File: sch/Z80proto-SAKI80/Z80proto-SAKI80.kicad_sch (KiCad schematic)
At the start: 21 parts, among them SW2 ABORT, U2 HC74, U20 AC00, U3 HC14, U7 2764, U8 628128, U9 HC138, X1 ACO-4.000MHz

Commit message: add SAKI80 support
add SAKI80(AKA Super AKI-80) support,
Modify Comand & intel HEX upload command to MiniLoader.
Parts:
- removed U3: HC14, symbol 74xx:74HC14
- removed X1: ACO-4.000MHz, Oscillator:Oscillator_DIP-14, symbol Oscillator:ACO-xxxMHz
- added U3: HC14, symbol 74xx:74LS14
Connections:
- net BUSAK*: now also U20.10
- net BUSNMI*: now also U3.3
- net BUSRES*: now also U3.11
- net BUSφ: now also U3.2
- net CPUφ: now also U3.13
- net GND: now also U3.10, U3.7 (GND), U3.9; no longer U20.1, U20.10, U20.2, U20.9
- net HALT: now also U20.3; no longer U20.11
- net HALT*: now also U20.1, U20.2; no longer U20.12, U20.13
- net NMI*: now also U3.6
- net RESET: now also U3.10, U3.9
- net VCC: now also U3.14 (VCC)
- net WR*: now also U20.12, U20.13
- net SYSRESET* renamed P3
- net P3: now also U3.8
- new net: U20.11, U20.9
- new net: U3.1, U3.12
- new net: U3.4, U3.5
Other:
- note added: "(or 2816)"
- note added: "26"
- note added: "A11(WR*)"
- note added: "Experimental: ROMKICK"
- note added: "NC(VCC)"
- note removed: "26(24)"
- note removed: "Evaluation: ROMKICK"
- moved on the sheet: C2, D2, R4, R5, SW2, U20A, U20C, U20D

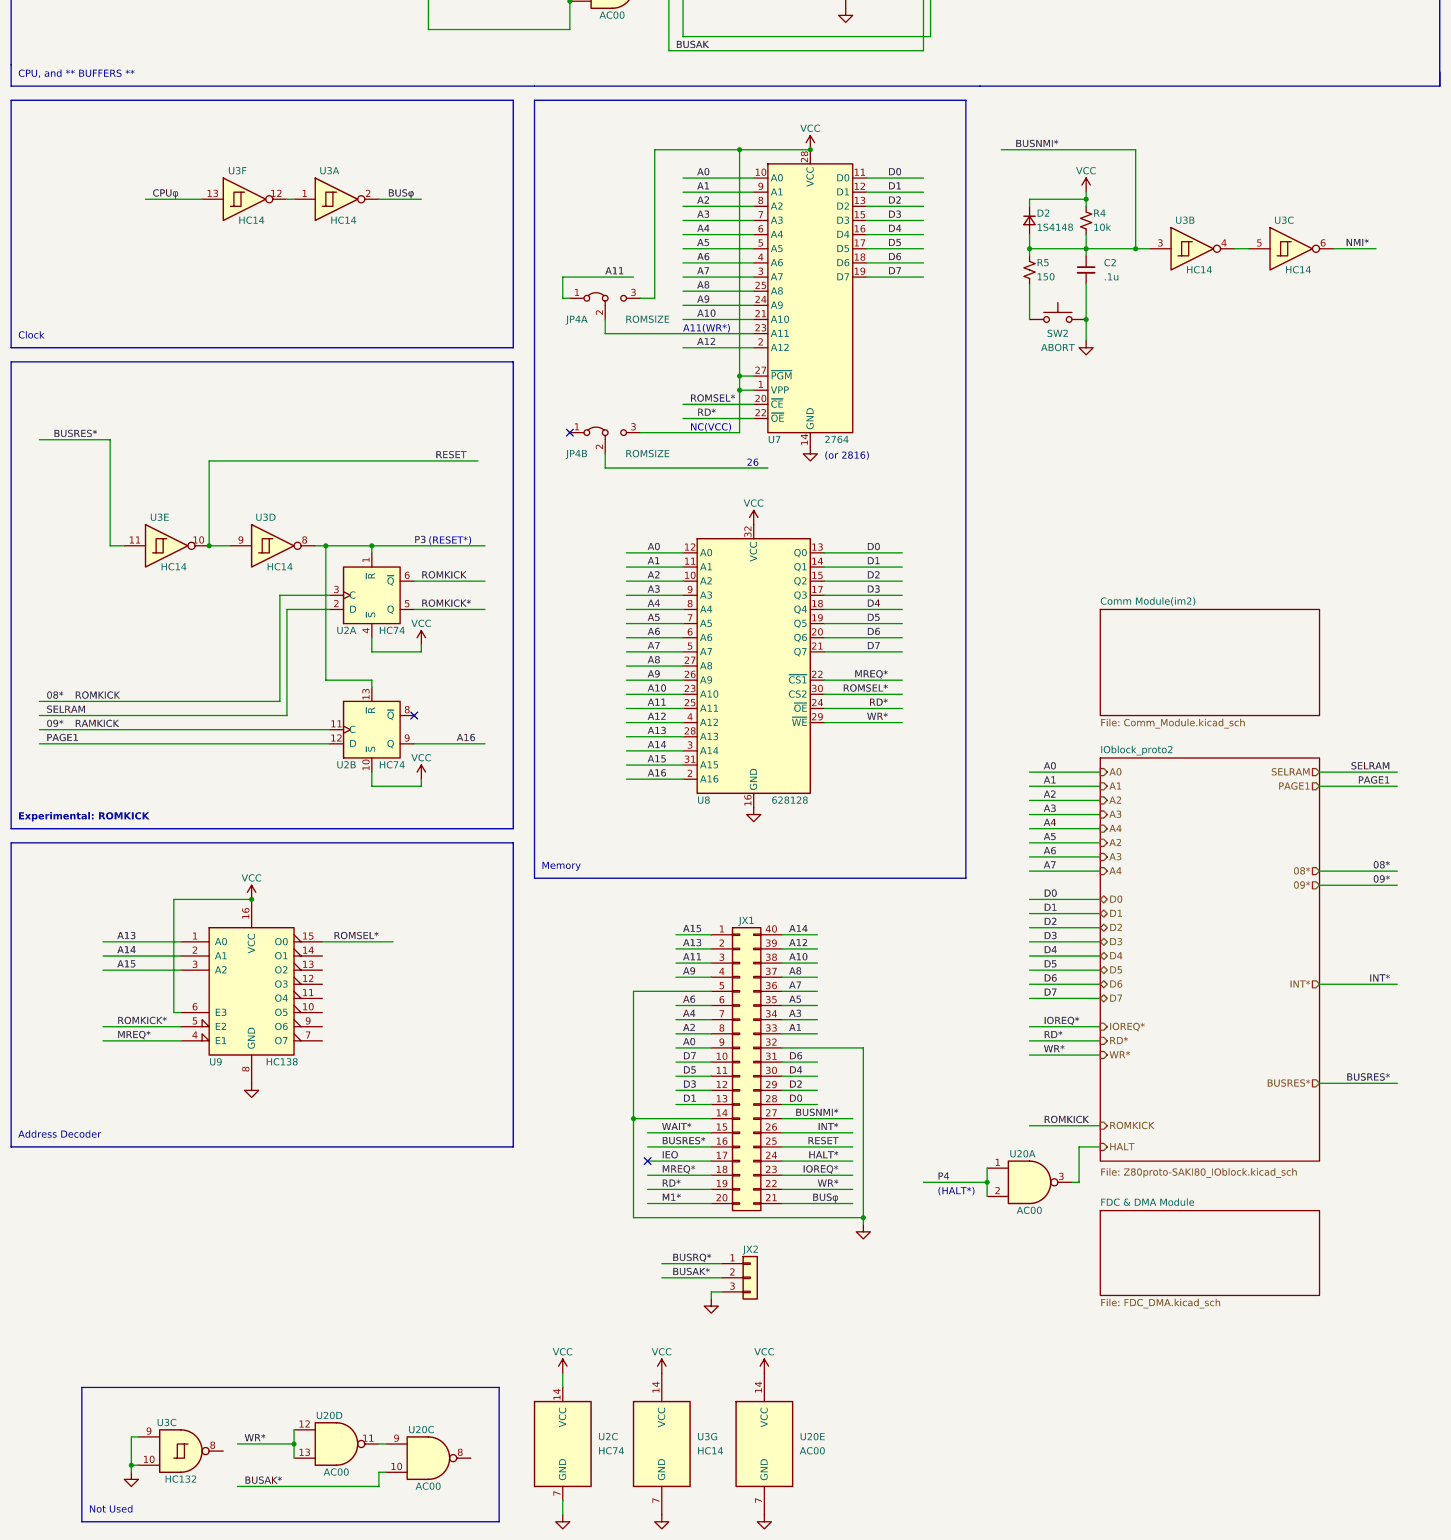
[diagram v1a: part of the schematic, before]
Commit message: add misc.
add SIO Hard flow control(but not work ...),
add WAIT implement,
add kermit implement(test).
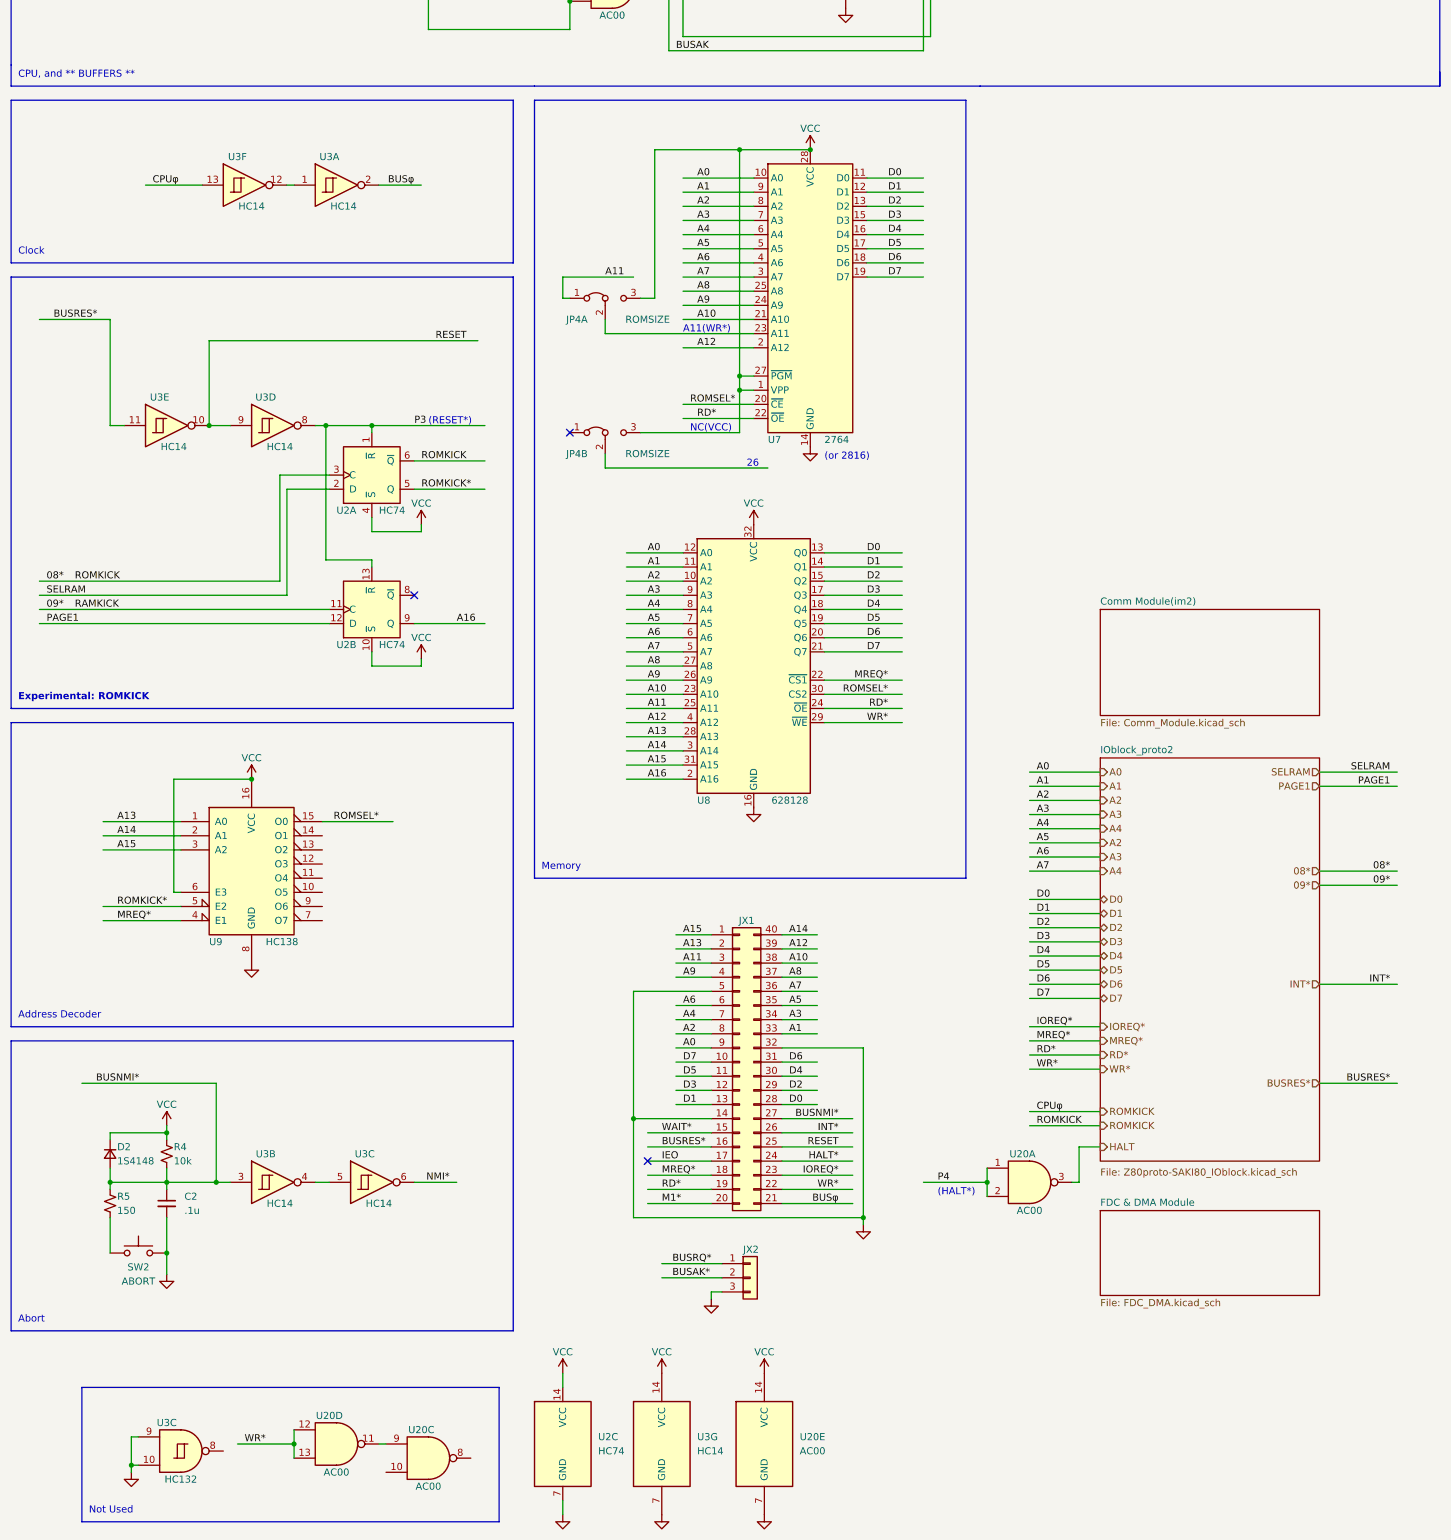
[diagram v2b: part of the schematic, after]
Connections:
- net CPUφ is gone; now on net 08*: U3.13, UB1.2 (~{CLKOUT})
- net BUSAK*: no longer U20.10
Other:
- note added: "Abort"
- moved on the sheet: C2, D2, R4, R5, SW2, U2A, U2B, U3A, U3B, U3C, U3D, U3E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

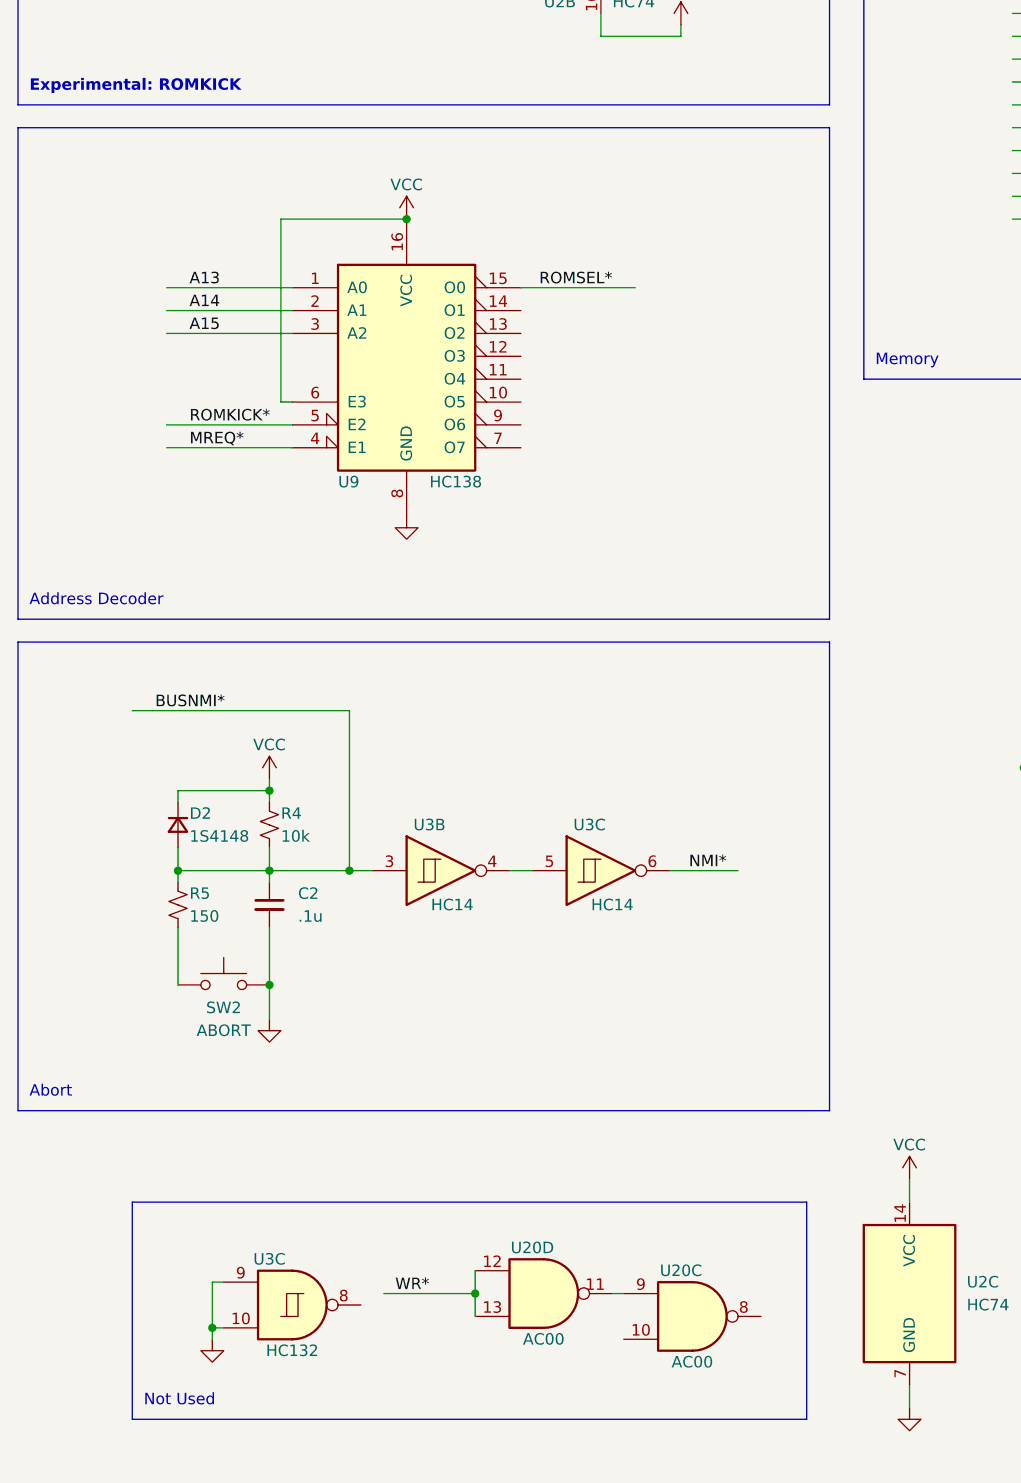
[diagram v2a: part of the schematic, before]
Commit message: patch xymodem.c and command_x.asm
add putchar_SIO0()/getchar_SIO0(), and SlowTick, SysTick
fix file title, comments
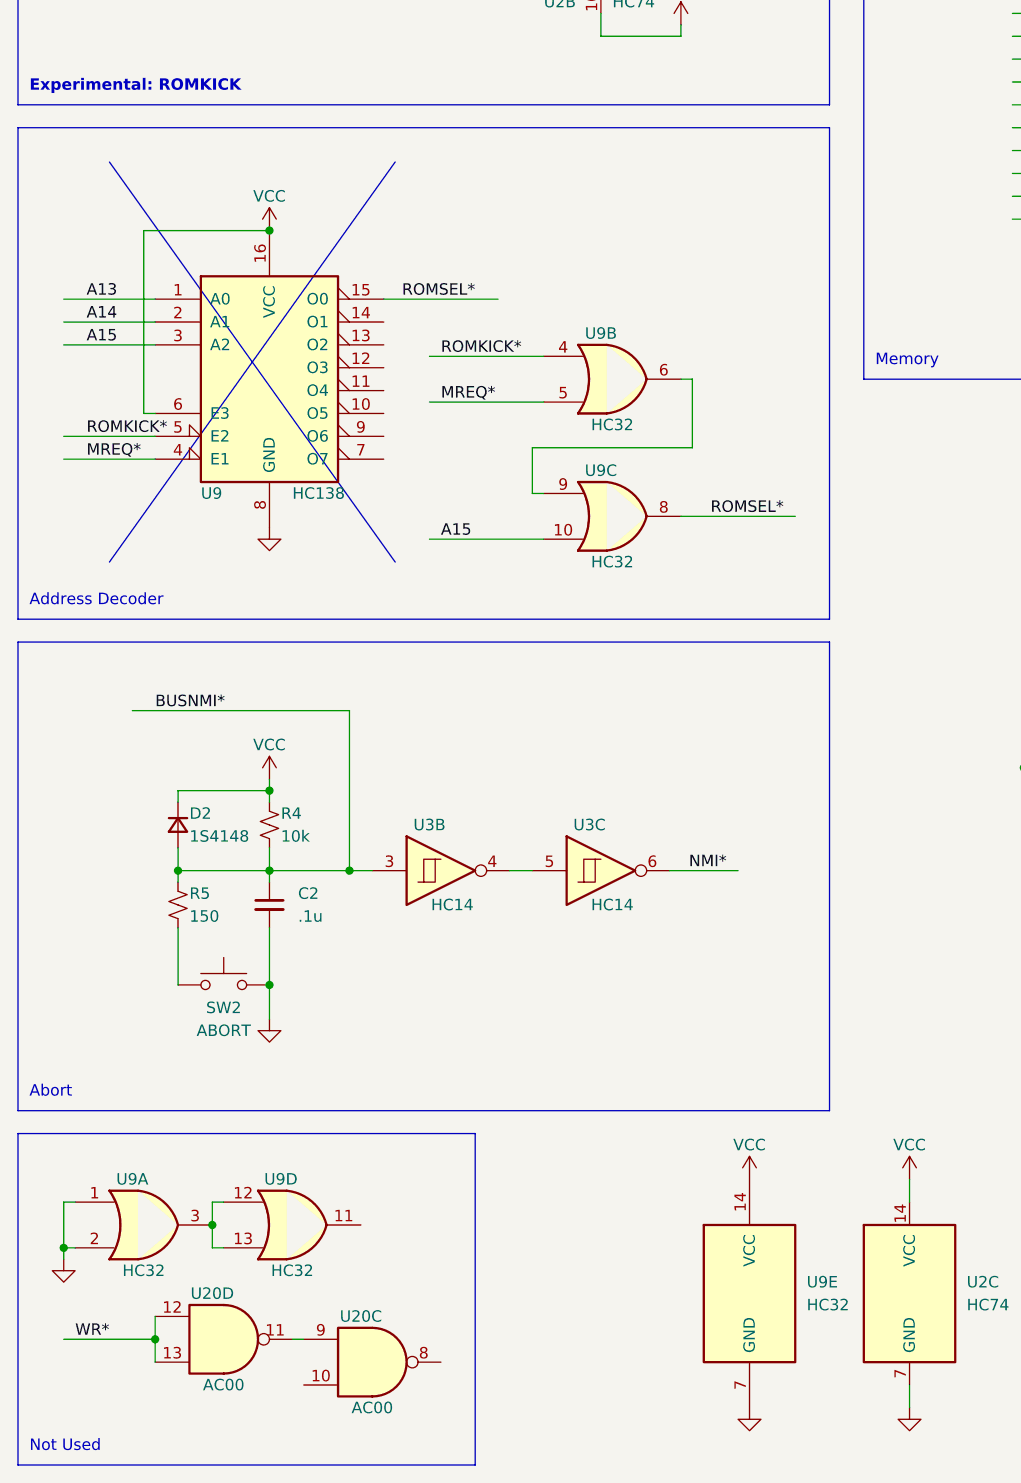
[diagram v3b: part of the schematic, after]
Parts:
- removed U3: HC132, symbol 74xx:74LS132
- added unit 2 of U9
- added unit 3 of U9
- added unit 5 of U9
- added unit 4 of U9
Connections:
- net A15: now also U9.10
- net GND: now also U9.1, U9.2, U9.7 (GND)
- net MREQ*: now also U9.5
- net ROMKICK*: now also U9.4
- net ROMSEL*: now also U9.8
- net VCC: now also U9.14 (VCC)
- new net: U9.6, U9.9
- new net: U9.12, U9.13, U9.3
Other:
- moved on the sheet: U20C, U20D, U9
